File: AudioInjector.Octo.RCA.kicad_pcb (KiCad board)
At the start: 2 copper layers, 58.5 x 43.9 mm, 66 parts, among them P5 DAC_out, P6 ADC_in, U20 AV6-8.4-13, U21 AV8-8.4-13

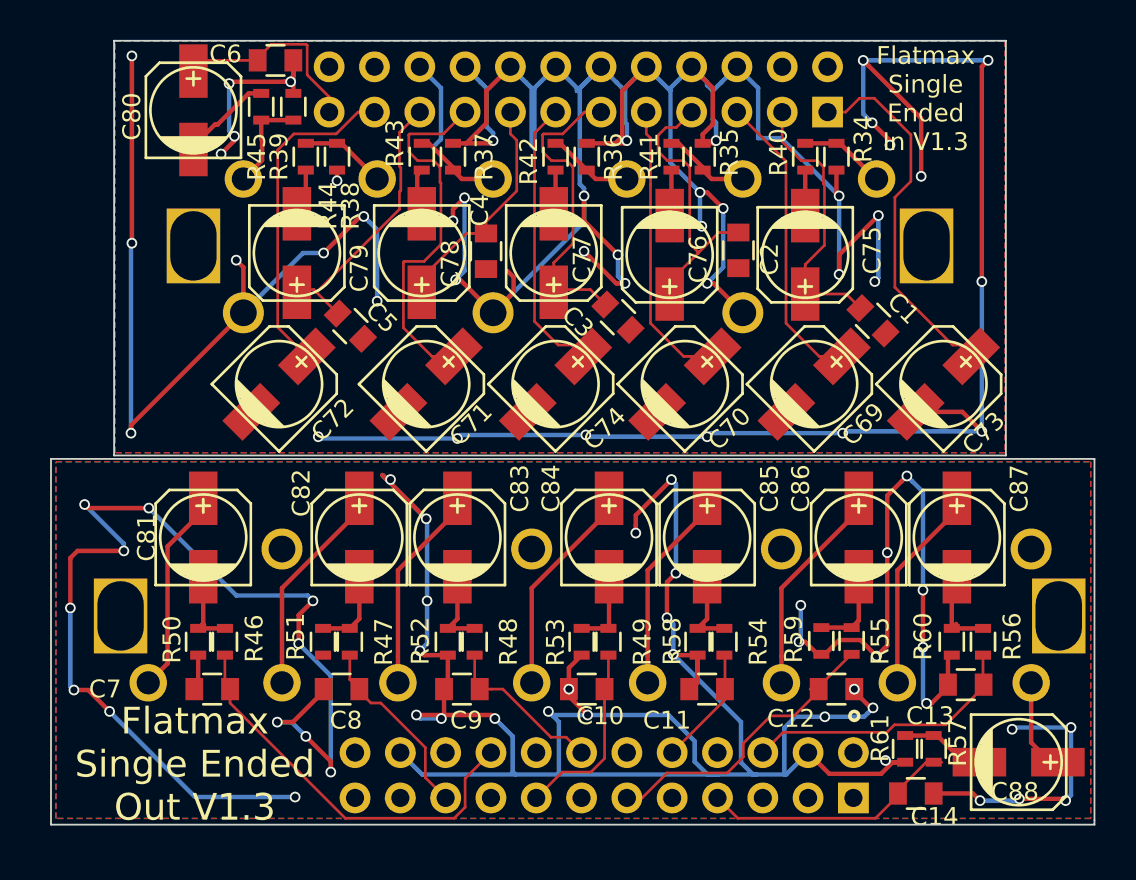
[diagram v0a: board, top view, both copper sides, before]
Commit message: Fixed a bug in the output circuit. Updated part values.
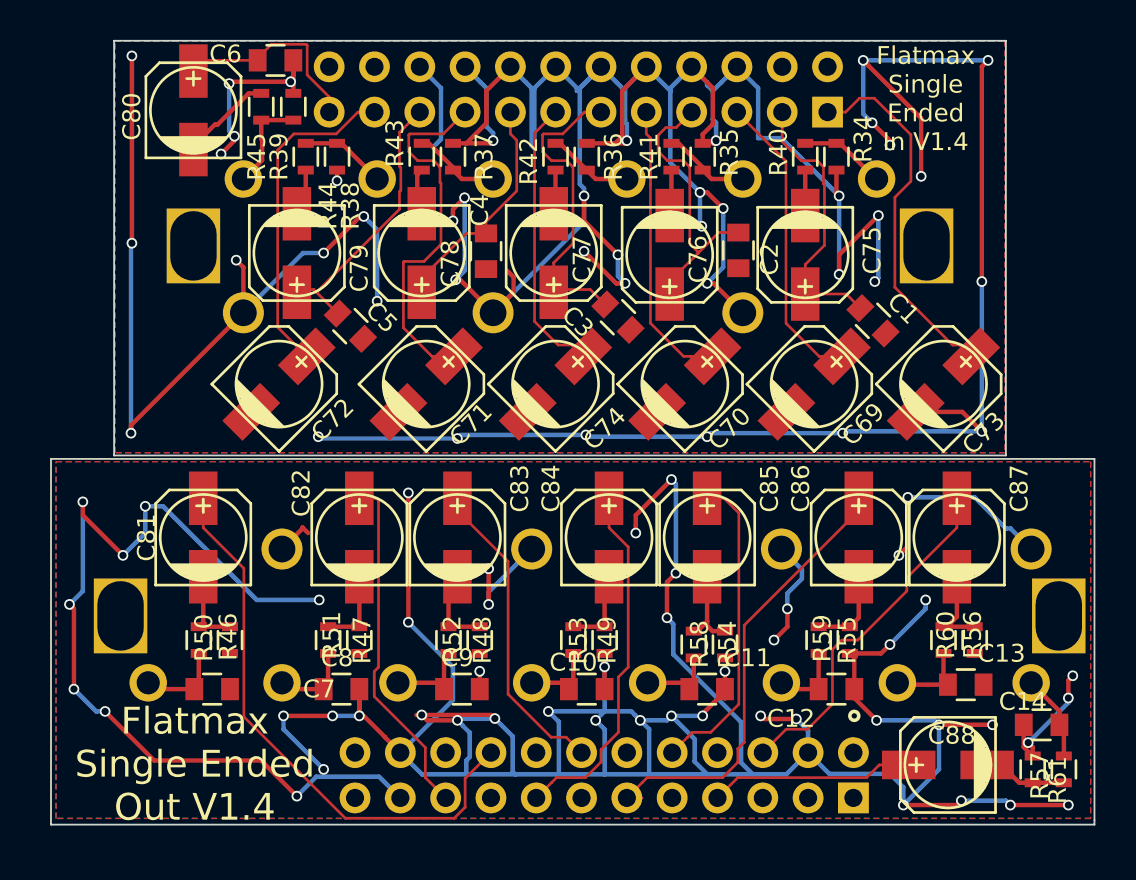
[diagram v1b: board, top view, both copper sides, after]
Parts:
- C81, C82, C83, C84, C85, C86, C87, C88: value 3.3u -> 10u
- R46, R47, R48, R49, R54, R55, R56, R57: value 560 -> 562
- moved C14 8.03 mm to (172.5, 165.0), turned to 180 degrees
- moved R57 7.39 mm to (173.8, 167.5), turned to 90 degrees
- moved R61 7.24 mm to (172.0, 167.5), turned to 90 degrees
- moved C88 3.97 mm to (167.2, 167.2), turned to 180 degrees
- moved R56 2.22 mm to (167.0, 160.2)
- moved R51 2.04 mm to (134.2, 160.2)
- moved R49 1.97 mm to (146.2, 160.2)
- moved R55 1.85 mm to (160.0, 160.2)
- moved R50 1.79 mm to (127.0, 160.2)
- moved R52 1.79 mm to (141.0, 160.2)
- moved R54 1.72 mm to (153.0, 160.5)
- moved R59 1.60 mm to (161.8, 160.2)
- moved R58 1.54 mm to (154.8, 160.5)
- moved R46 1.47 mm to (125.2, 160.2)
- moved R48 1.47 mm to (139.2, 160.2)
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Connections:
- net /ADC_fb1+ renamed /Codec/ADC_fb1+
- net /ADC_fb1- renamed /Codec/ADC_fb1-
- net /ADC_fb2+ renamed /Codec/ADC_fb2+
- net /ADC_fb2- renamed /Codec/ADC_fb2-
- net /ADC_fb3+ renamed /Codec/ADC_fb3+
- net /ADC_fb3- renamed /Codec/ADC_fb3-
- net /ADC_fb4+ renamed /Codec/ADC_fb4+
- net /ADC_fb4- renamed /Codec/ADC_fb4-
- net /ADC_fb5+ renamed /Codec/ADC_fb5+
- net /ADC_fb5- renamed /Codec/ADC_fb5-
- net /ADC_fb6+ renamed /Codec/ADC_fb6+
- net /ADC_fb6- renamed /Codec/ADC_fb6-
- net /In1 renamed /Codec/In1
- net /In2 renamed /Codec/In2
- net /In3 renamed /Codec/In3
- net /In4 renamed /Codec/In4
- net /In5 renamed /Codec/In5
- net /In6 renamed /Codec/In6
- C1 pad 2: /AGND -> /Codec/AGND
- C10 pad 1: /AOUT4+ -> /Codec/Out4
- C10 pad 2: /AGND -> /Codec/AGND
- C11 pad 1: /AOUT5+ -> /Codec/Out5
- C11 pad 2: /AGND -> /Codec/AGND
- C12 pad 1: /AOUT6+ -> /Codec/Out6
- C12 pad 2: /AGND -> /Codec/AGND
- C13 pad 1: /AOUT7+ -> /Codec/Out7
- C13 pad 2: /AGND -> /Codec/AGND
- C14 pad 1: /AOUT8+ -> /Codec/Out8
- C14 pad 2: /AGND -> /Codec/AGND
- C2 pad 2: /AGND -> /Codec/AGND
- C3 pad 2: /AGND -> /Codec/AGND
- C4 pad 2: /AGND -> /Codec/AGND
- C5 pad 2: /AGND -> /Codec/AGND
- C6 pad 2: /AGND -> /Codec/AGND
- C69 pad 2: /AGND -> /Codec/AGND
- C7 pad 1: /AOUT1+ -> /Codec/Out1
- C7 pad 2: /AGND -> /Codec/AGND
- C70 pad 2: /AGND -> /Codec/AGND
- C71 pad 2: /AGND -> /Codec/AGND
- C72 pad 2: /AGND -> /Codec/AGND
- C73 pad 2: /AGND -> /Codec/AGND
- C74 pad 2: /AGND -> /Codec/AGND
- C8 pad 1: /AOUT2+ -> /Codec/Out2
- C8 pad 2: /AGND -> /Codec/AGND
- C81 pad 1: /Out1 -> /Codec/AOUT1+
- C82 pad 1: /Out2 -> /Codec/AOUT2+
- C83 pad 1: /Out3 -> /Codec/AOUT3+
- C84 pad 1: /Out4 -> /Codec/AOUT4+
- C85 pad 1: /Out5 -> /Codec/AOUT5+
- C86 pad 1: /Out6 -> /Codec/AOUT6+
- C87 pad 1: /Out7 -> /Codec/AOUT7+
- C88 pad 1: /Out8 -> /Codec/AOUT8+
- C9 pad 1: /AOUT3+ -> /Codec/Out3
- C9 pad 2: /AGND -> /Codec/AGND
- P5 pad 10: /AOUT5+ -> /Codec/AOUT5+
- P5 pad 11: /AOUT6+ -> /Codec/AOUT6+
- P5 pad 14: /AOUT3+ -> /Codec/AOUT3+
- P5 pad 15: /AOUT4+ -> /Codec/AOUT4+
- P5 pad 18: /AOUT1+ -> /Codec/AOUT1+
- P5 pad 19: /AOUT2+ -> /Codec/AOUT2+
- P5 pad 21: /AGND -> /Codec/AGND
- P5 pad 22: /AGND -> /Codec/AGND
- P5 pad 4: /AGND -> /Codec/AGND
- P5 pad 6: /AOUT7+ -> /Codec/AOUT7+
- P5 pad 7: /AOUT8+ -> /Codec/AOUT8+
- P6 pad 10: /AGND -> /Codec/AGND
- P6 pad 12: /AGND -> /Codec/AGND
- P6 pad 14: /AGND -> /Codec/AGND
- P6 pad 16: /AGND -> /Codec/AGND
- P6 pad 18: /AGND -> /Codec/AGND
- P6 pad 20: /AGND -> /Codec/AGND
- P6 pad 6: /AGND -> /Codec/AGND
- P6 pad 8: /AGND -> /Codec/AGND
- R34 pad 2: /AGND -> /Codec/AGND
- R35 pad 2: /AGND -> /Codec/AGND
- R36 pad 2: /AGND -> /Codec/AGND
- R37 pad 2: /AGND -> /Codec/AGND
- R38 pad 2: /AGND -> /Codec/AGND
- R39 pad 2: /AGND -> /Codec/AGND
- R46 pad 2: /AOUT1+ -> /Codec/Out1
- R47 pad 2: /AOUT2+ -> /Codec/Out2
- R48 pad 2: /AOUT3+ -> /Codec/Out3
- R49 pad 2: /AOUT4+ -> /Codec/Out4
- R50 pad 2: /AGND -> /Codec/AGND
- R51 pad 2: /AGND -> /Codec/AGND
- R52 pad 2: /AGND -> /Codec/AGND
- R53 pad 2: /AGND -> /Codec/AGND
- R54 pad 2: /AOUT5+ -> /Codec/Out5
- R55 pad 2: /AOUT6+ -> /Codec/Out6
- R56 pad 2: /AOUT7+ -> /Codec/Out7
- R57 pad 2: /AOUT8+ -> /Codec/Out8
- R58 pad 2: /AGND -> /Codec/AGND
- R59 pad 2: /AGND -> /Codec/AGND
- R60 pad 2: /AGND -> /Codec/AGND
- R61 pad 2: /AGND -> /Codec/AGND
- U20 pad 1: /AGND -> /Codec/AGND
- U20 pad 4: /AGND -> /Codec/AGND
- U20 pad 7: /AGND -> /Codec/AGND
- U21 pad 1: /AGND -> /Codec/AGND
- U21 pad 10: /AGND -> /Codec/AGND
- U21 pad 11: /Out7 -> /Codec/Out7
- U21 pad 12: /Out8 -> /Codec/Out8
- U21 pad 2: /Out1 -> /Codec/Out1
- U21 pad 3: /Out2 -> /Codec/Out2
- U21 pad 4: /AGND -> /Codec/AGND
- U21 pad 5: /Out3 -> /Codec/Out3
- U21 pad 6: /Out4 -> /Codec/Out4
- U21 pad 7: /AGND -> /Codec/AGND
- U21 pad 8: /Out5 -> /Codec/Out5
- U21 pad 9: /Out6 -> /Codec/Out6
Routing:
- net /Codec/AGND: track 0.00 -> 542.5 mm, vias 0 -> 91
- net /AGND: track 520.2 -> 0.00 mm, vias 86 -> 0
- net /Codec/AOUT1+: track 0.00 -> 32.6 mm
- net /Codec/AOUT6+: track 0.00 -> 25.5 mm
- net /AOUT1+: track 22.6 -> 0.00 mm
- net /Codec/AOUT4+: track 0.00 -> 21.0 mm
- net /Codec/AOUT7+: track 0.00 -> 20.7 mm
- net /Codec/AOUT2+: track 0.00 -> 20.3 mm
- net /Codec/AOUT5+: track 0.00 -> 18.4 mm
- net /Codec/AOUT3+: track 0.00 -> 17.6 mm
- net /AOUT6+: track 17.3 -> 0.00 mm
- net /AOUT7+: track 15.7 -> 0.00 mm
- net /AOUT8+: track 14.4 -> 0.00 mm
- net /Out6: track 12.1 -> 0.00 mm
- net /Out2: track 12.1 -> 0.00 mm
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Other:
- board text added: "Flatmax Single Ended In V1.4"
- board text added: "Flatmax Single Ended Out V1.4"
- board text removed: "Flatmax Single Ended In V1.3"
- board text removed: "Flatmax Single Ended Out V1.3"

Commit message: Adding v1.5 of these PCBs.
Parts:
- moved R61 1.85 mm to (173.8, 167.4)
- moved R57 1.60 mm to (172.2, 167.4)
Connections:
- P5 pad 10: /Codec/AOUT5+ -> (no net)
- P5 pad 11: /Codec/AOUT6+ -> (no net)
- P5 pad 12: (no net) -> /Codec/AOUT6+
- P5 pad 13: (no net) -> /Codec/AOUT3+
- P5 pad 14: /Codec/AOUT3+ -> (no net)
- P5 pad 15: /Codec/AOUT4+ -> (no net)
- P5 pad 16: (no net) -> /Codec/AOUT4+
- P5 pad 17: (no net) -> /Codec/AOUT1+
- P5 pad 18: /Codec/AOUT1+ -> (no net)
- P5 pad 19: /Codec/AOUT2+ -> (no net)
- P5 pad 20: (no net) -> /Codec/AOUT2+
- P5 pad 3: (no net) -> /Codec/AGND
- P5 pad 4: /Codec/AGND -> (no net)
- P5 pad 5: (no net) -> /Codec/AOUT7+
- P5 pad 6: /Codec/AOUT7+ -> (no net)
- P5 pad 7: /Codec/AOUT8+ -> (no net)
- P5 pad 8: (no net) -> /Codec/AOUT8+
- P5 pad 9: (no net) -> /Codec/AOUT5+
- P6 pad 1: /Codec/ADC_fb1- -> V5
- P6 pad 10: /Codec/AGND -> /Codec/ADC_fb3-
- P6 pad 11: /Codec/ADC_fb3+ -> /Codec/AGND
- P6 pad 12: /Codec/AGND -> /Codec/ADC_fb3+
- P6 pad 13: /Codec/ADC_fb4- -> /Codec/AGND
- P6 pad 14: /Codec/AGND -> /Codec/ADC_fb4-
- P6 pad 15: /Codec/ADC_fb4+ -> /Codec/AGND
- P6 pad 16: /Codec/AGND -> /Codec/ADC_fb4+
- P6 pad 17: /Codec/ADC_fb5- -> /Codec/AGND
- P6 pad 18: /Codec/AGND -> /Codec/ADC_fb5-
- P6 pad 19: /Codec/ADC_fb5+ -> /Codec/AGND
- P6 pad 2: V5 -> /Codec/ADC_fb1-
- P6 pad 20: /Codec/AGND -> /Codec/ADC_fb5+
- P6 pad 21: /Codec/ADC_fb6- -> V5
- P6 pad 22: V5 -> /Codec/ADC_fb6-
- P6 pad 23: /Codec/ADC_fb6+ -> V5
- P6 pad 24: V5 -> /Codec/ADC_fb6+
- P6 pad 3: /Codec/ADC_fb1+ -> V5
- P6 pad 4: V5 -> /Codec/ADC_fb1+
- P6 pad 5: /Codec/ADC_fb2- -> /Codec/AGND
- P6 pad 6: /Codec/AGND -> /Codec/ADC_fb2-
- P6 pad 7: /Codec/ADC_fb2+ -> /Codec/AGND
- P6 pad 8: /Codec/AGND -> /Codec/ADC_fb2+
- P6 pad 9: /Codec/ADC_fb3- -> /Codec/AGND
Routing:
- net /Codec/AGND: track 542.5 -> 476.1 mm, vias 91 -> 87
- net /Codec/ADC_fb3-: track 16.2 -> 24.6 mm
- net /Codec/ADC_fb4-: track 15.8 -> 20.2 mm
- net /Codec/ADC_fb5-: track 20.8 -> 24.8 mm
- net /Codec/AOUT8+: track 11.5 -> 15.0 mm
- net /Codec/ADC_fb4+: track 14.0 -> 17.4 mm
- net /Codec/ADC_fb5+: track 16.1 -> 19.4 mm
- net /Codec/AOUT3+: track 17.6 -> 20.6 mm
- net /Codec/ADC_fb2-: track 16.9 -> 19.7 mm
- net /Codec/AOUT2+: track 20.3 -> 17.6 mm
- net /Codec/ADC_fb6+: track 11.4 -> 8.83 mm
- net /Codec/ADC_fb2+: track 16.2 -> 18.6 mm
- net /Codec/ADC_fb6-: track 18.5 -> 20.7 mm
- net /Codec/AOUT7+: track 20.7 -> 22.8 mm
- net /Codec/AOUT6+: track 25.5 -> 27.5 mm
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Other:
- outline, holes or cut-outs redrawn
- board text added: "Flatmax RCA In V1.5"
- board text added: "Flatmax RCA Out V1.5"
- board text added: "audioinjector.net"
- board text removed: "Flatmax Single Ended In V1.4"
- board text removed: "Flatmax Single Ended Out V1.4"
